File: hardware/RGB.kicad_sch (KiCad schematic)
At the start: 28 parts

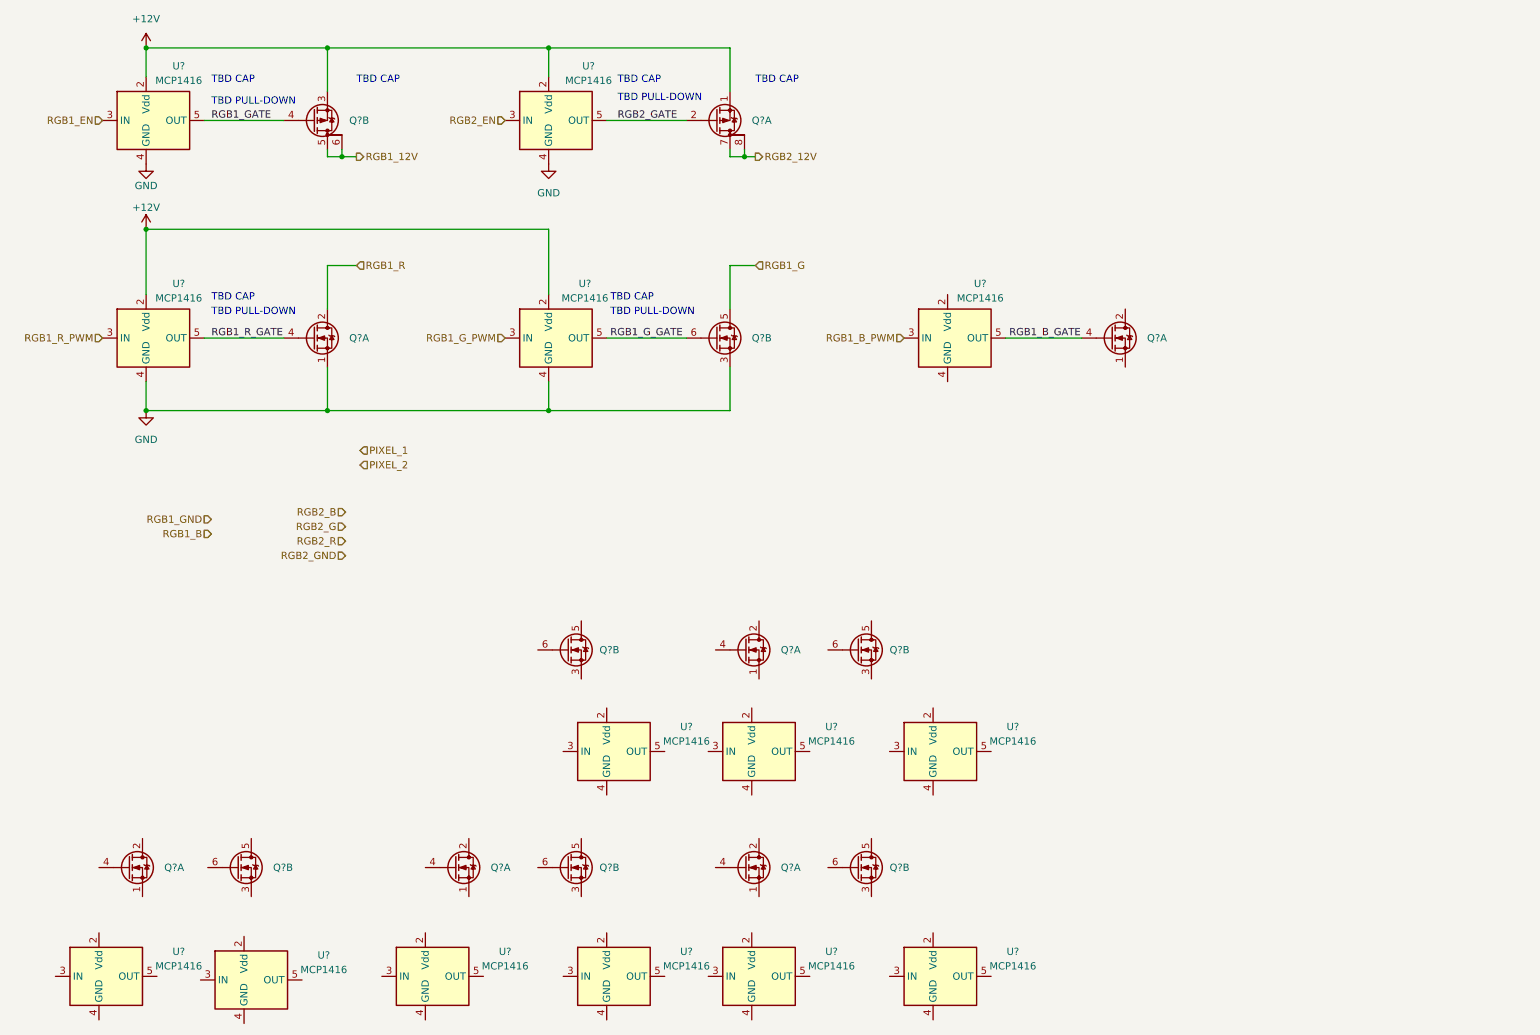
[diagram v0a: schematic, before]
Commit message: Schematic updates: stm32 sheet
Signed-off-by: Connor Rigby <connorr@hey.com>
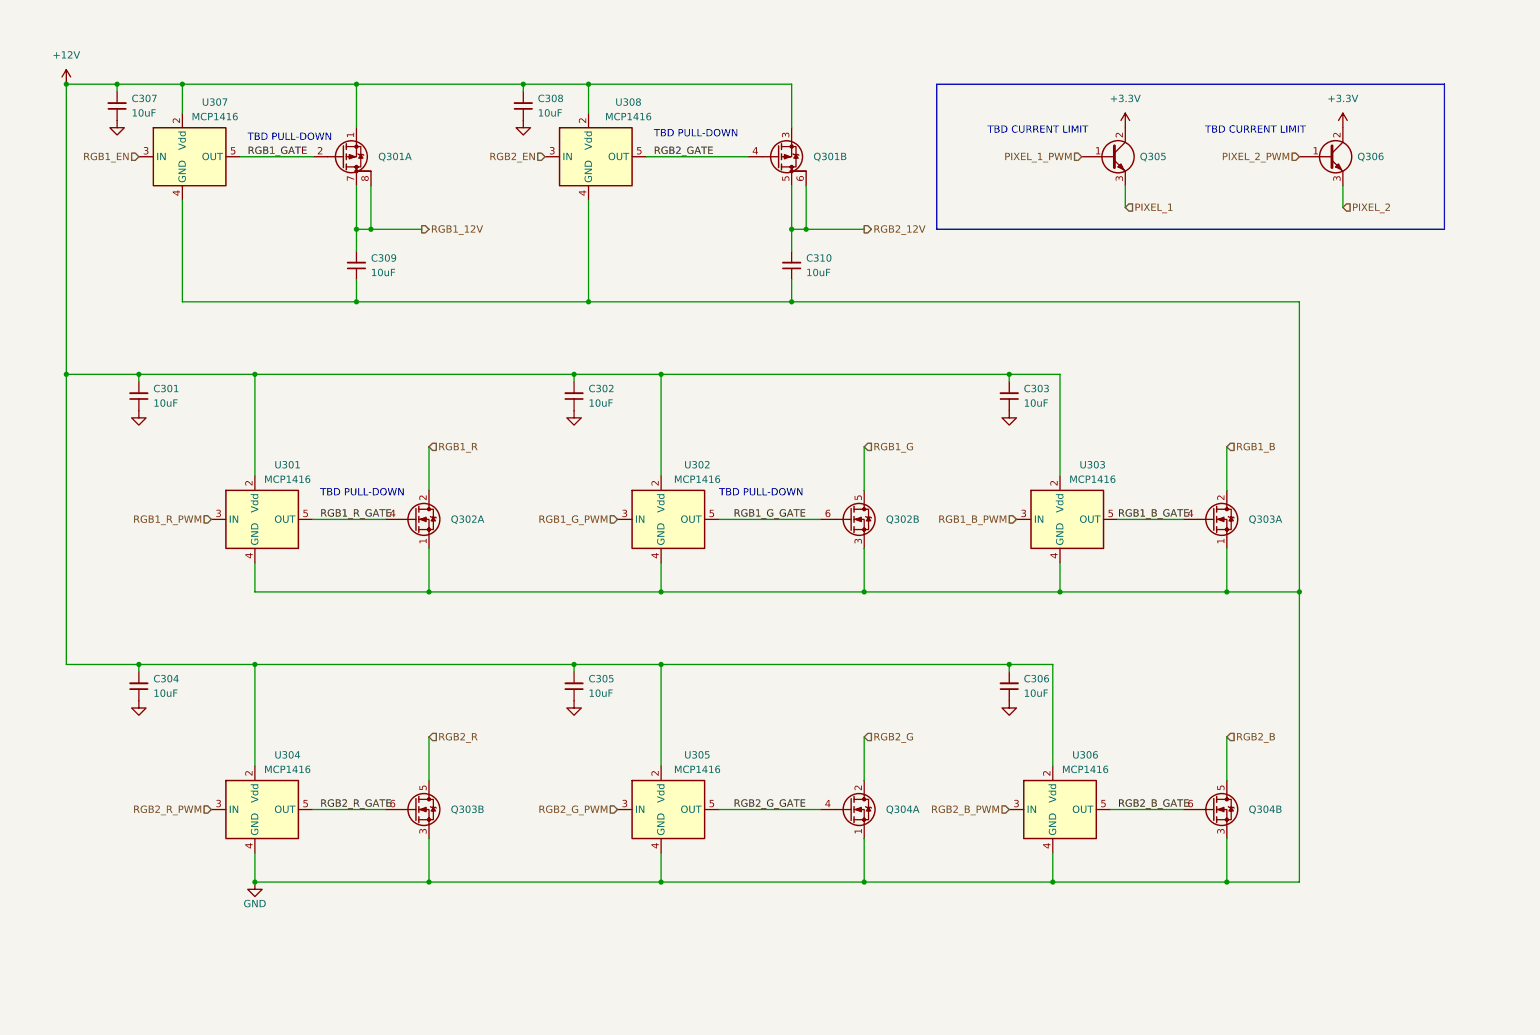
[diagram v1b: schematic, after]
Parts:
- removed Q? (x6): 8205A, Package_TO_SOT_SMD:SOT-23-6, symbol LCSC_MOSFET:8205A
- removed U? (x9): MCP1416, Package_TO_SOT_SMD:SOT-23-5, symbol LCSC_MOSFET:MCP1416
- added C301, C302, C303, C304, C305, C306, C307, C308, C309, C310: C_0805_10u_X5R, Capacitor_SMD:C_0805_2012Metric, symbol LCSC_Capacitor:C_0805_10u_X5R
- added Q305, Q306: BCX56, Package_TO_SOT_SMD:SOT-89-3, symbol LCSC_Transistor:BCX56
- added U304, U305, U306: MCP1416, Package_TO_SOT_SMD:SOT-23-5, symbol LCSC_MOSFET:MCP1416
- gave numbers to parts that had none: 9
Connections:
- net +12V: now also U303.2 (Vdd), C301.2, C302.2, C303.2, C304.2, C305.2, C306.2, C307.2, C308.2, U304.2 (Vdd), U305.2 (Vdd), U306.2 (Vdd)
- net GND: now also Q303.1 (S), Q303.3 (S), Q304.1 (S), Q304.3 (S), U303.4 (GND), C301.1, C302.1, C303.1, C304.1, C305.1, C306.1, C307.1, C308.1, C309.1, C310.1, U304.4 (GND), U305.4 (GND), U306.4 (GND)
- net PIXEL_1: now also Q305.3 (E)
- net PIXEL_2: now also Q306.3 (E)
- net RGB1_12V: now also Q301.7 (D), Q301.8 (G), C309.2; no longer Q301.5 (D), Q301.6 (G)
- net RGB1_B: now also Q303.2 (D)
- net RGB1_GATE: now also Q301.2 (G); no longer Q301.4 (G)
- net RGB2_12V: now also Q301.5 (D), Q301.6 (G), C310.2; no longer Q301.7 (D), Q301.8 (G)
- net RGB2_B: now also Q304.5 (D)
- net RGB2_G: now also Q304.2 (D)
- net RGB2_GATE: now also Q301.4 (G); no longer Q301.2 (G)
- net RGB2_R: now also Q303.5 (D)
- net RGB2_R_GATE: now reaches Q303.6 (G)
- net RGB2_R_GATE: now also U304.5 (OUT)
- net RGB2_B_GATE: now reaches Q304.6 (G)
- net RGB2_B_GATE: now also U306.5 (OUT)
- net RGB2_G_GATE: now reaches Q304.4 (G)
- net RGB2_G_GATE: now also U305.5 (OUT)
- new net +3.3V: Q305.2 (C), Q306.2 (C)
- new net PIXEL_1_PWM: Q305.1 (B)
- new net PIXEL_2_PWM: Q306.1 (B)
- new net RGB2_B_PWM: U306.3 (IN)
- new net RGB2_G_PWM: U305.3 (IN)
- new net RGB2_R_PWM: U304.3 (IN)
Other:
- note added: "TBD CURRENT LIMIT"
- note removed: "TBD CAP"
- moved on the sheet: Q301A, Q301B, Q302A, Q302B, Q303A, Q303B, Q304A, Q304B, U301, U302, U303, U307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

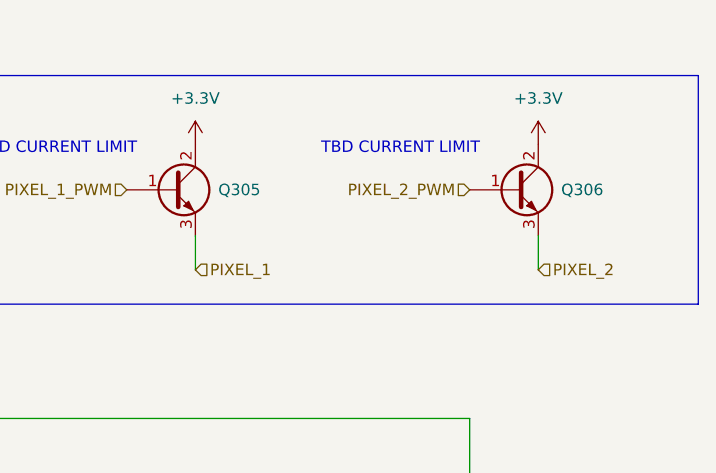
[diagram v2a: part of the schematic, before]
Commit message: RF layout updates
Signed-off-by: Connor Rigby <connorr@hey.com>
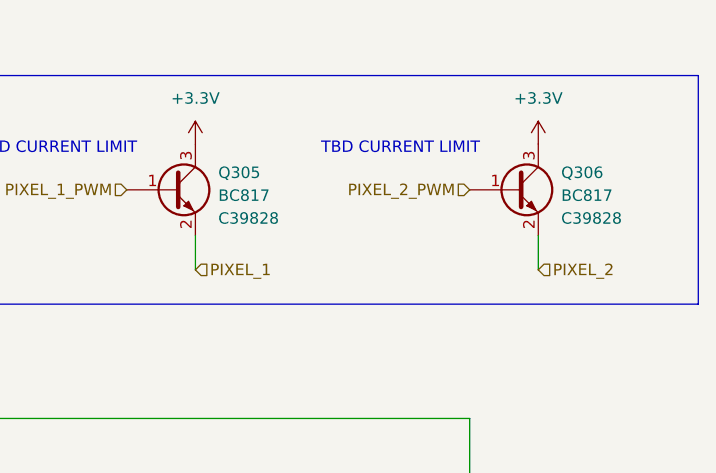
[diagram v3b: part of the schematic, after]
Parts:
- removed Q305, Q306: BCX56, Package_TO_SOT_SMD:SOT-89-3, symbol LCSC_Transistor:BCX56
- added Q305, Q306: BC817, Package_TO_SOT_SMD:SOT-23, symbol LCSC_Transistor1:BC817
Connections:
- net +3.3V: now also Q305.3 (C), Q306.3 (C)
- net PIXEL_1: now also Q305.2 (E)
- net PIXEL_1_PWM: now also Q305.1 (B)
- net PIXEL_2: now also Q306.2 (E)
- net PIXEL_2_PWM: now also Q306.1 (B)
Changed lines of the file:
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@@
-    )
-  )
-  (symbol (lib_id "LCSC_Transistor:BCX56") (at 246.38 38.1 0) (unit 1)
-    (in_bom yes) (on_board yes) (dnp no) (fields_autoplaced)
-    (property "Reference" "Q306" (at 251.46 38.0999 0)
-      (effects (font (size 1.27 1.27)) (justify left))
-    )
-    (property "Value" "BCX56" (at 251.46 39.37 0)
-      (effects (font (size 1.27 1.27)) (justify left) hide)
-    )
-    (property "Footprint" "Package_TO_SOT_SMD:SOT-89-3" (at 251.46 35.56 0)
-      (effects (font (size 1.27 1.27)) hide)
-    )
-    (property "Datasheet" "https://datasheet.lcsc.com/lcsc/1811011112_Jiangsu-Changjing-Electronics-Technology-Co---Ltd--BCX56_C24280.pdf" (at 246.38 38.1 0)
-      (effects (font (size 1.27 1.27)) hide)
-    )
-    (property "LCSC" "C24280" (at 246.38 38.1 0)
-      (effects (font (size 1.27 1.27)) hide)
-    )
-    (property "MPN" "BCX56" (at 246.38 38.1 0)
-      (effects (font (size 1.27 1.27)) hide)
-    )
-    (pin "1")
-    (pin "2")
-    (pin "3")
-    (instances
-      (project "underglow2"
-        (path "/dcbdf88a-d6ac-4b1d-9514-0b0ce113d90b/d698d388-4189-4a55-a8ce-744fe305194e"
-          (reference "Q306") (unit 1)
-        )
-      )
     )
   )
@@
     )
   )
+  (symbol (lib_id "LCSC_Transistor1:BC817") (at 246.38 38.1 0) (unit 1)
+    (in_bom yes) (on_board yes) (dnp no) (fields_autoplaced)
+    (property "Reference" "Q306" (at 251.46 36.195 0)
+      (effects (font (size 1.27 1.27)) (justify left))
+    )
+    (property "Value" "BC817" (at 251.46 38.735 0)
+      (effects (font (size 1.27 1.27)) (justify left))
+    )
+    (property "Footprint" "Package_TO_SOT_SMD:SOT-23" (at 251.46 40.005 0)
+      (effects (font (size 1.27 1.27) italic) (justify left) hide)
+    )
+    (property "Datasheet" "https://www.onsemi.com/pub/Collateral/BC818-D.pdf" (at 246.38 38.1 0)
+      (effects (font (size 1.27 1.27)) (justify left) hide)
+    )
+    (property "LCSC" "C39828" (at 251.46 41.275 0)
+      (effects (font (size 1.27 1.27)) (justify left))
+    )
+    (pin "1")
+    (pin "2")
+    (pin "3")
+    (instances
+      (project "underglow2"
+        (path "/dcbdf88a-d6ac-4b1d-9514-0b0ce113d90b/d698d388-4189-4a55-a8ce-744fe305194e"
+          (reference "Q306") (unit 1)
+        )
+      )
+    )
+  )
   (symbol (lib_id "LCSC_Capacitor:C_0805_10u_X5R") (at 38.1 80.01 180) (unit 1)
     (in_bom yes) (on_board yes) (dnp no) (fields_autoplaced)
@@
     )
   )
-  (symbol (lib_id "LCSC_Transistor:BCX56") (at 208.28 38.1 0) (unit 1)
-    (in_bom yes) (on_board yes) (dnp no) (fields_autoplaced)
-    (property "Reference" "Q305" (at 213.36 38.0999 0)
-      (effects (font (size 1.27 1.27)) (justify left))
-    )
-    (property "Value" "BCX56" (at 213.36 39.37 0)
-      (effects (font (size 1.27 1.27)) (justify left) hide)
-    )
-    (property "Footprint" "Package_TO_SOT_SMD:SOT-89-3" (at 213.36 35.56 0)
-      (effects (font (size 1.27 1.27)) hide)
-    )
-    (property "Datasheet" "https://datasheet.lcsc.com/lcsc/1811011112_Jiangsu-Changjing-Electronics-Technology-Co---Ltd--BCX56_C24280.pdf" (at 208.28 38.1 0)
-      (effects (font (size 1.27 1.27)) hide)
-    )
-    (property "LCSC" "C24280" (at 208.28 38.1 0)
-      (effects (font (size 1.27 1.27)) hide)
-    )
-    (property "MPN" "BCX56" (at 208.28 38.1 0)
-      (effects (font (size 1.27 1.27)) hide)
-    )
-    (pin "1")
-    (pin "2")
-    (pin "3")
-    (instances
-      (project "underglow2"
-        (path "/dcbdf88a-d6ac-4b1d-9514-0b0ce113d90b/d698d388-4189-4a55-a8ce-744fe305194e"
-          (reference "Q305") (unit 1)
-        )
-      )
-    )
-  )
   (symbol (lib_id "LCSC_Capacitor:C_0805_10u_X5R") (at 34.29 29.21 180) (unit 1)
     (in_bom yes) (on_board yes) (dnp no) (fields_autoplaced)
@@
         )
       )
+    )
+  )
+  (symbol (lib_id "LCSC_Transistor1:BC817") (at 208.28 38.1 0) (unit 1)
+    (in_bom yes) (on_board yes) (dnp no) (fields_autoplaced)
+    (property "Reference" "Q305" (at 213.36 36.195 0)
+      (effects (font (size 1.27 1.27)) (justify left))
+    )
+    (property "Value" "BC817" (at 213.36 38.735 0)
+      (effects (font (size 1.27 1.27)) (justify left))
+    )
+    (property "Footprint" "Package_TO_SOT_SMD:SOT-23" (at 213.36 40.005 0)
+      (effects (font (size 1.27 1.27) italic) (justify left) hide)
+    )
+    (property "Datasheet" "https://www.onsemi.com/pub/Collateral/BC818-D.pdf" (at 208.28 38.1 0)
+      (effects (font (size 1.27 1.27)) (justify left) hide)
+    )
+    (property "LCSC" "C39828" (at 213.36 41.275 0)
+      (effects (font (size 1.27 1.27)) (justify left))
+    )
+    (pin "1")
+    (pin "2")
+    (pin "3")
+    (instances
+      (project "underglow2"
+        (path "/dcbdf88a-d6ac-4b1d-9514-0b0ce113d90b/d698d388-4189-4a55-a8ce-744fe305194e"
+          (reference "Q305") (unit 1)
+        )
+      )

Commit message: Pre-production updates
Signed-off-by: Connor Rigby <connorr@hey.com>
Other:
- company: (none) -> https://cone.codes
- title: (none) -> coneRGB2
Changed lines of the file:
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@@
 (kicad_sch (version 20230121) (generator eeschema)
   (paper "A4")
+  (title_block
+    (title "coneRGB2")
+    (date "2023-03-20")
+    (rev "1")
+    (company "https://cone.codes")
+    (comment 1 "https://github.com/connorrigby/underglow2")
+    (comment 2 "Designed by Connor Rigby")
+    (comment 3 "Handles translating TTL level PWM from the microcontroller and output +12v signals ")
+    (comment 4 "RGB and NZR Output")
+  )
   (junction (at 165.1 114.3) (diameter 0) (color 0 0 0 0)
   )
@@
     (stroke (width 0) (type default))
   )
+  (text_box "Transistor for protection of the MCU pins"
+    (at 180.34 43.18 0) (size 26.67 5.08)
+    (stroke (width 0) (type default))
+    (fill (type none))
+    (effects (font (size 1.27 1.27)) (justify left top))
+  )
+  (text_box "6 total PWM-able, 12V low side outputs and 2 12V high side outputs.\nIntended to represent two \"channels\" of RGB both with 1 high and 3 low side outputs.\n"
+    (at 21.59 173.99 0) (size 57.15 10.16)
+    (stroke (width 0) (type default))
+    (fill (type none))
+    (effects (font (size 1.27 1.27)) (justify left top))
+  )
   (text "TBD PULL-DOWN" (at 57.15 35.56 0)

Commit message: Rev 2 submitted for production
Signed-off-by: Connor Rigby <connorr@hey.com>
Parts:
- removed Q305, Q306: BC817, Package_TO_SOT_SMD:SOT-23, symbol LCSC_Transistor1:BC817
- added D202 (x2): 30v 230mv@100ma 1A, Diode_SMD:D_SOD-323F, symbol Device:D_Schottky
- added R301, R302: R_0603_100k, Resistor_SMD:R_0603_1608Metric, symbol LCSC_Resistor:R_0603_100k
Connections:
- net GND: now also R301.2, R302.2
- net PIXEL_1: now also D202.1 (K)
- net PIXEL_2: now also D202.1 (K)
- net RGB1_B_PWM renamed CH1_B_PWM
- net RGB1_EN renamed CH1_EN_PWM
- net CH1_EN_PWM: now also R301.1
- net RGB1_G_PWM renamed CH1_G_PWM
- net RGB1_R_PWM renamed CH1_R_PWM
- net RGB2_B_PWM renamed CH2_B_PWM
- net RGB2_EN renamed CH2_EN_PWM
- net CH2_EN_PWM: now also R302.1
- net RGB2_G_PWM renamed CH2_G_PWM
- net RGB2_R_PWM renamed CH2_R_PWM
- new net CH1_NZR: D202.2 (A)
- new net CH2_NZR: D202.2 (A)
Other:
- note removed: "TBD CURRENT LIMIT"
- moved on the sheet: C301, C302, C303, C304, C305, C306, C307, C308, C309, C310, Q301A, Q301B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

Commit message: asdf
Signed-off-by: Connor Rigby <connorr@hey.com>
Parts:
- removed C301, C302, C303, C304, C305, C306, C307, C308, C309, C310: C_0805_10u_X5R, Capacitor_SMD:C_0805_2012Metric, symbol LCSC_Capacitor:C_0805_10u_X5R
- removed Q301: AO4803A, Package_SO:SOP-8_3.76x4.96mm_P1.27mm, symbol LCSC_MOSFET:AO4803A
- removed Q302, Q303, Q304: 8205A, Package_TO_SOT_SMD:SOT-23-6, symbol LCSC_MOSFET:8205A
- removed U304, U305, U306, U307, U308: MCP1416, Package_TO_SOT_SMD:SOT-23-5, symbol LCSC_MOSFET:MCP1416
- added C301, C302, C303: C_0805_1u_X7R, Capacitor_SMD:C_0805_2012Metric, symbol LCSC_Capacitor:C_0805_1u_X7R
- added Q301: Q_PMOS_GDS, Package_TO_SOT_SMD:TO-252-2, symbol Device:Q_PMOS_GDS
- added Q302, Q303, Q304: Q_NMOS_GDS, Package_TO_SOT_SMD:SOT-223-3_TabPin2, symbol Device:Q_NMOS_GDS
- added R303, R304: R_0603_100k, Resistor_SMD:R_0603_1608Metric, symbol LCSC_Resistor:R_0603_100k
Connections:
- net CH2_EN_PWM is gone; now on net R_PWM_IN: R302.1
- net +12V: now also Q301.2 (D); no longer U301.2 (Vdd), U302.2 (Vdd), U303.2 (Vdd)
- net GND: now also C301.2, C302.2, C303.2, R303.2, R304.2
- net CH1_B_PWM renamed B_PWM_IN
- net B_PWM_IN: now also R304.1
- net CH1_EN_PWM renamed RGB_EN
- net RGB_EN: now also Q301.1 (G)
- net CH1_G_PWM renamed G_PWM_IN
- net G_PWM_IN: now also R303.1
- net CH1_NZR renamed NZR1_IN
- net CH1_R_PWM renamed R_PWM_IN
- net CH2_NZR renamed NZR2_IN
- net PIXEL_1 renamed NZR1_OUT
- net PIXEL_2 renamed NZR2_OUT
- net RGB1_B_GATE renamed B_GATE
- net B_GATE: now also Q304.1 (G)
- net RGB1_G_GATE renamed G_GATE
- net G_GATE: now also Q303.1 (G)
- net RGB1_R_GATE renamed R_GATE
- net R_GATE: now also Q302.1 (G)
- new net B_PWM_OUT: Q304.3 (S)
- new net G_PWM_OUT: Q303.3 (S)
- new net RGB_VOUT: C301.1, C302.1, C303.1, Q301.3 (S), Q302.2 (D), Q303.2 (D), Q304.2 (D), U301.2 (Vdd), U302.2 (Vdd), U303.2 (Vdd)
- new net R_PWM_OUT: Q302.3 (S)
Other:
- note removed: "TBD PULL-DOWN"
